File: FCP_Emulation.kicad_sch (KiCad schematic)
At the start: 92 parts, among them J1 Conn_01x10_Female, J2 Conn_01x10_Female, J3 Conn_01x10_Female, J4 Conn_01x02_Female, J5 Conn_01x02_Female, U2 LM2902

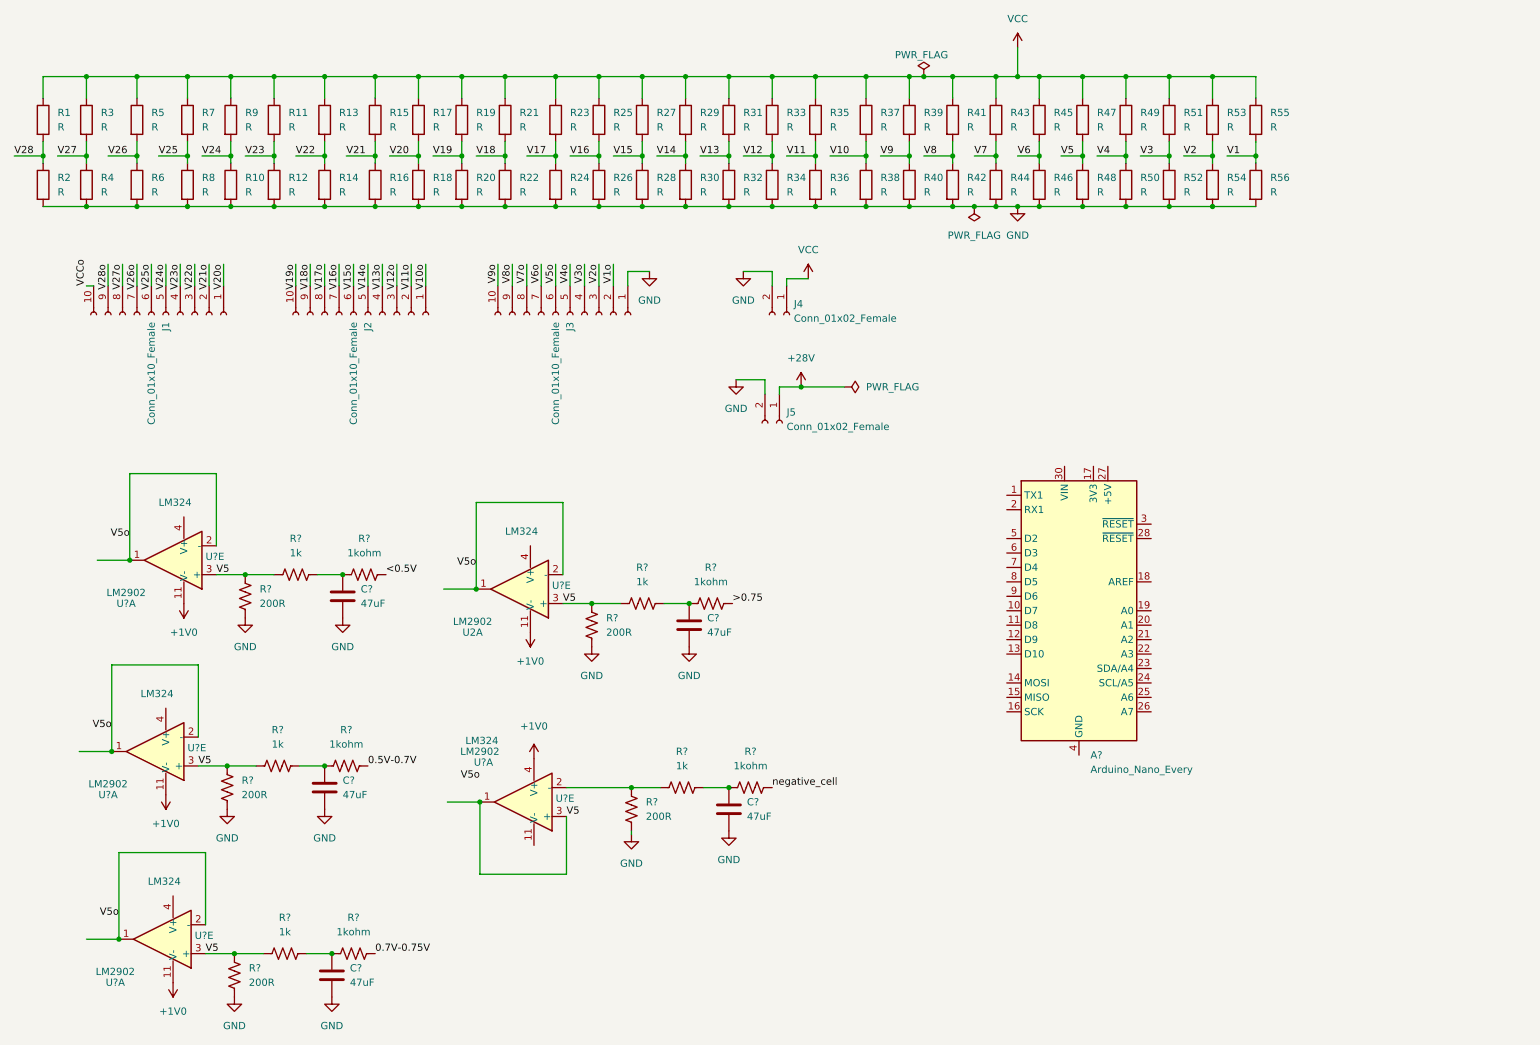
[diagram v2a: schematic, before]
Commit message: changed op amp circuit values based on breadboarding and simualtion
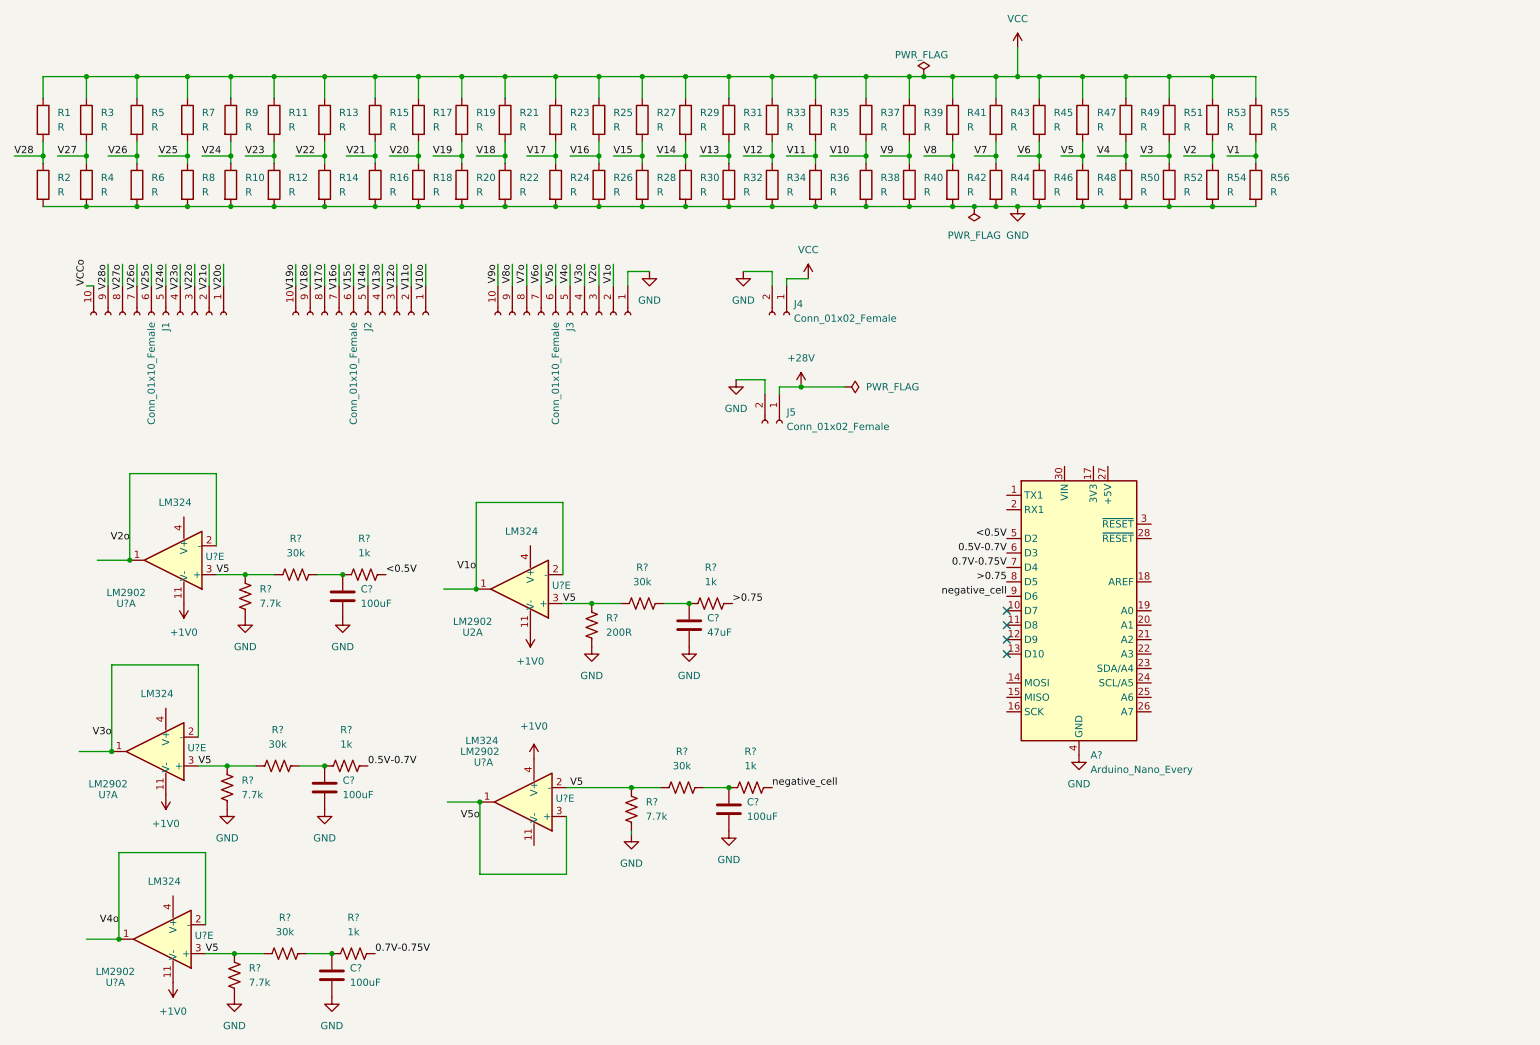
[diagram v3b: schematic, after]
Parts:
- C? (x4): value 47uF -> 100uF
- R? (x5): value 1kohm -> 1k
- R? (x4): value 200R -> 7.7k
- R? (x5): value 1k -> 30k
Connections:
- net 0.5V-0.7V: now also A?.6 (D3)
- net 0.7V-0.75V: now also A?.7 (D4)
- net <0.5V: now also A?.5 (D2)
- net >0.75: now also A?.8 (D5)
- net GND: now also A?.29 (GND), A?.4 (GND)
- net V1o: now also U2.1, U2.2 (-)
- net V2o: now also U?.1, U?.2 (-)
- net V3o: now also U?.1, U?.2 (-)
- net V4o: now also U?.1, U?.2 (-)
- net V5: now also R?.1, R?.1, U?.2 (-); no longer U?.1, U?.3 (+)
- net V5o: now also U?.1, U?.3 (+); no longer U2.1, U2.2 (-), U?.1, U?.1, U?.1, U?.2 (-), U?.2 (-), U?.2 (-)
- net negative_cell: now also A?.9 (D6)
- no-connect marks 0 -> 4

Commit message: added negative case schematic
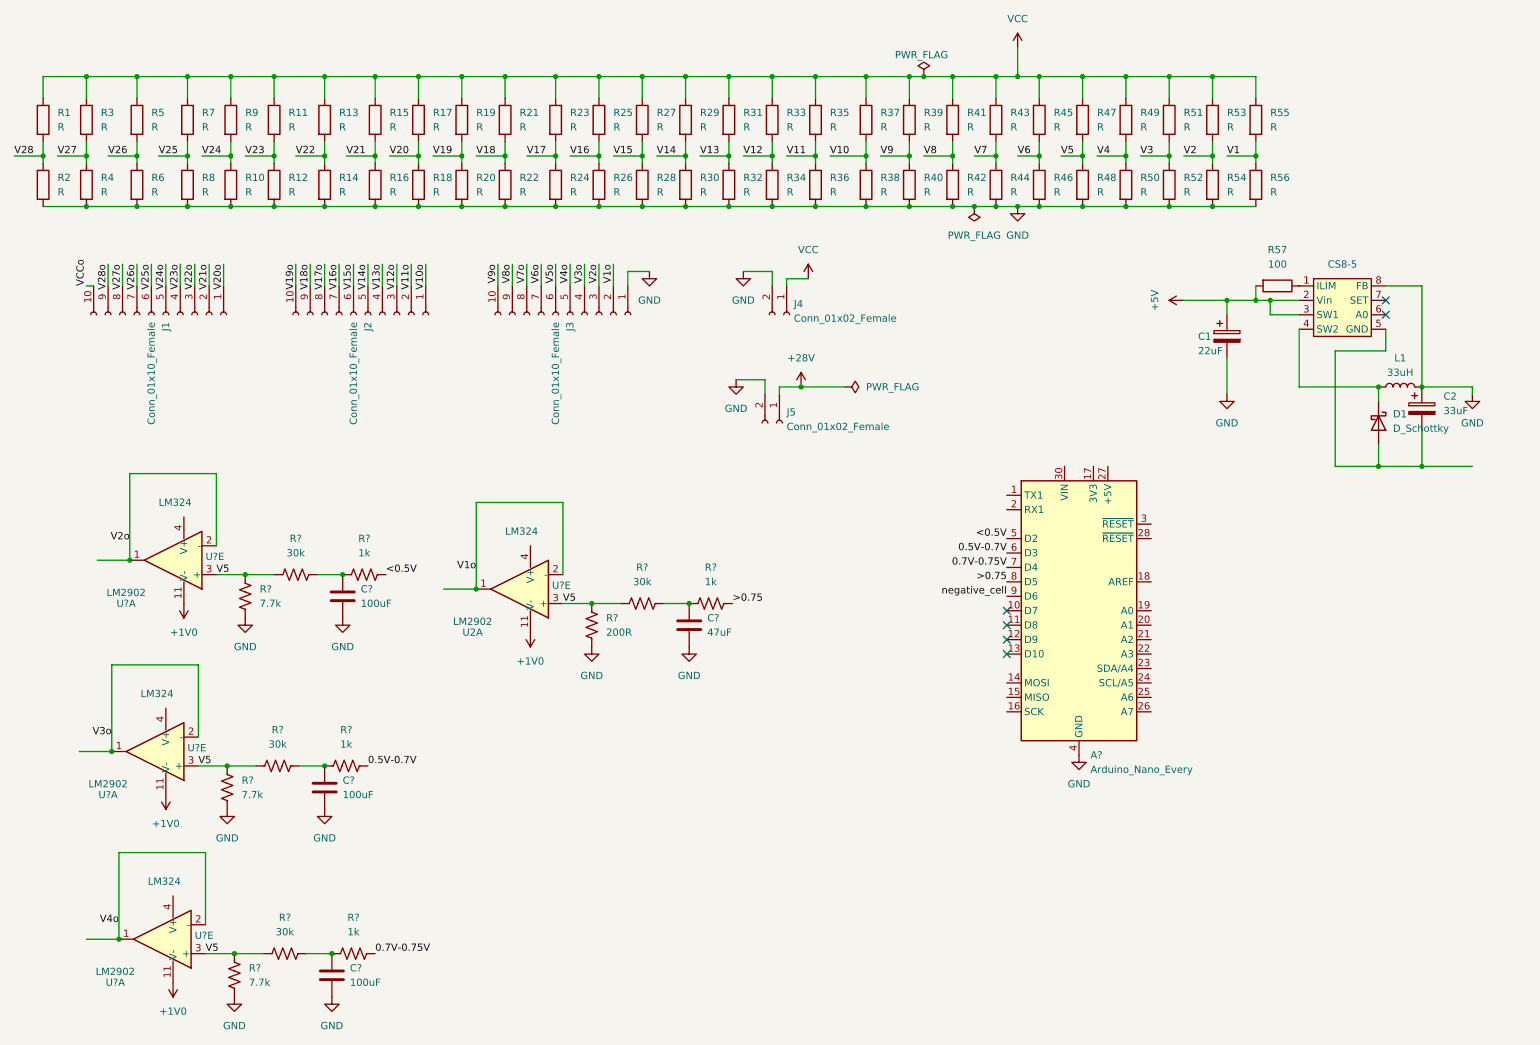
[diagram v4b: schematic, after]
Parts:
- removed C?: 100uF, symbol Device:C
- removed R?: 1k, symbol Device:R_US
- removed R?: 7.7k, symbol Device:R_US
- removed R?: 30k, symbol Device:R_US
- removed U?: LM2902, Package_SO:SO-14_3.9x8.65mm_P1.27mm, symbol Amplifier_Operational:LM2902
- removed U?: LM324, symbol Amplifier_Operational:LM324
- added C1: 22uF, symbol Device:C_Polarized
- added C2: 33uF, symbol Device:C_Polarized
- added CS8-5: ~, symbol lt1111:LT1111CN8-5
- added D1: D_Schottky, symbol Device:D_Schottky
- added L1: 33uH, symbol Device:L
- added R57: 100, symbol Device:R
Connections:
- net GND: now also C1.2, C2.1, CS8-5.8 (FB), L1.2
- new net: CS8-5.1 (ILIM), R57.1
- new net: CS8-5.4 (SW2), D1.1 (K), L1.1
- new net: C2.2, CS8-5.5 (GND), D1.2 (A)
- new net +5V: C1.1, CS8-5.2 (Vin), CS8-5.3 (SW1), R57.2
- no-connect marks 4 -> 6

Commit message: added voltage divider on negative case
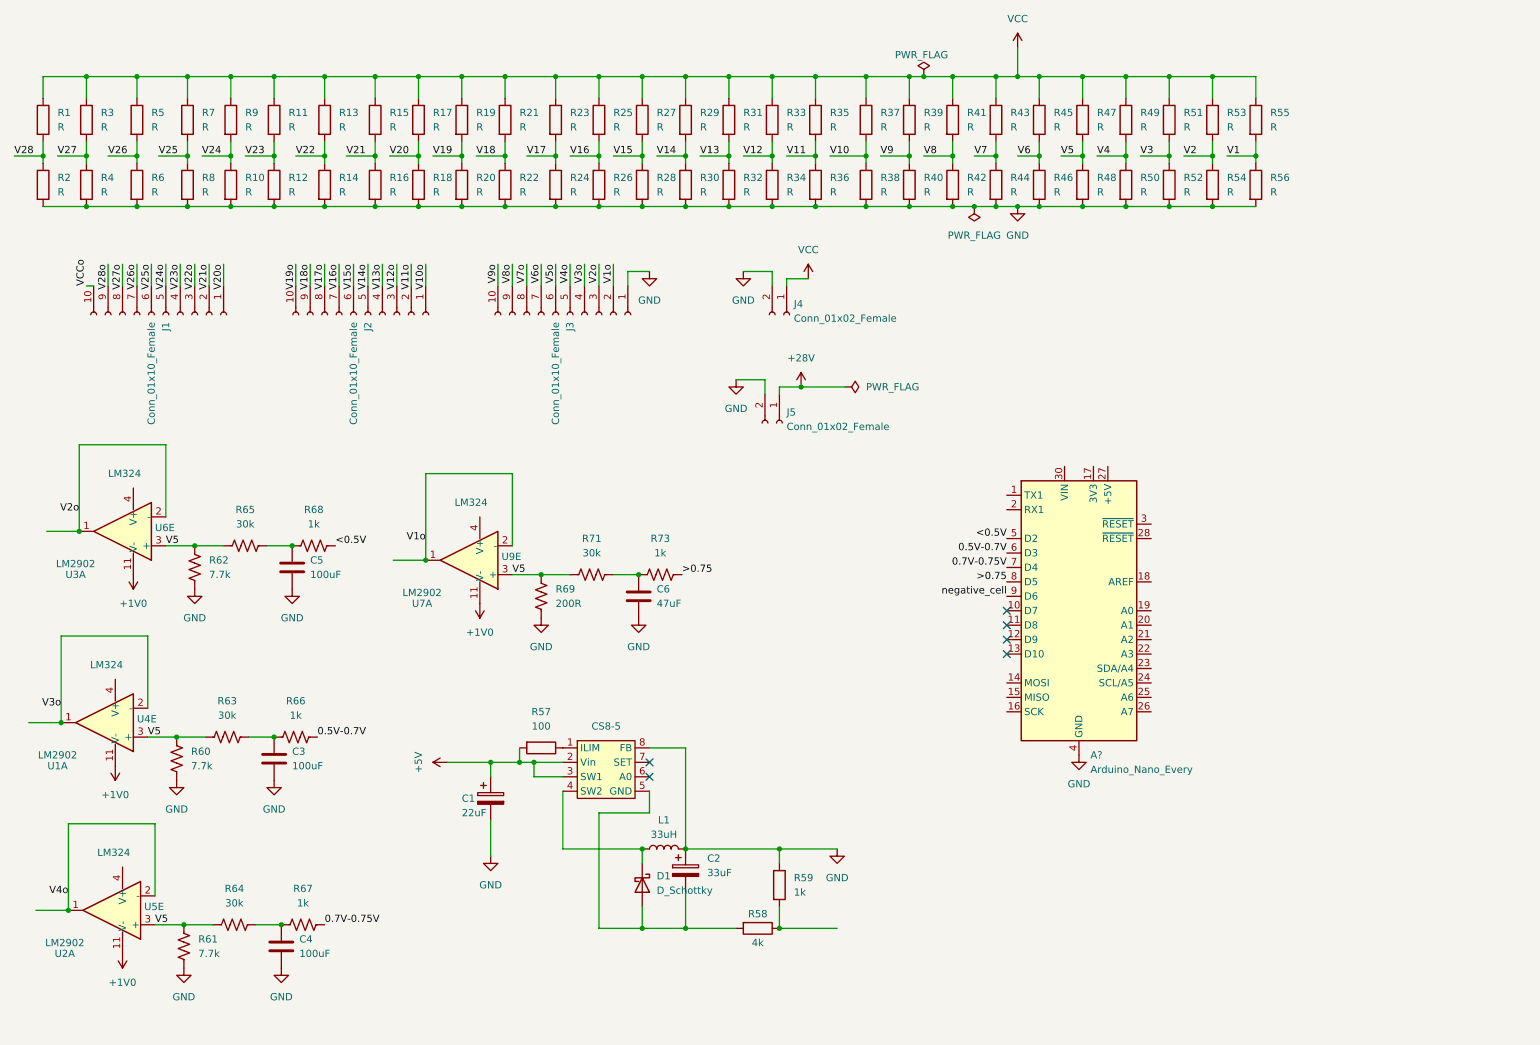
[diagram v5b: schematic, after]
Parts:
- removed C?: 47uF, symbol Device:C
- removed C? (x3): 100uF, symbol Device:C
- removed R? (x4): 1k, symbol Device:R_US
- removed R? (x3): 7.7k, symbol Device:R_US
- removed R? (x4): 30k, symbol Device:R_US
- removed R?: 200R, symbol Device:R_US
- removed U? (x4): LM324, symbol Amplifier_Operational:LM324
- removed U? (x3): LM2902, Package_SO:SO-14_3.9x8.65mm_P1.27mm, symbol Amplifier_Operational:LM2902
- added C3, C4, C5: 100uF, symbol Device:C
- added C6: 47uF, symbol Device:C
- added R58: 4k, symbol Device:R
- added R59: 1k, symbol Device:R
- added R60, R61, R62: 7.7k, symbol Device:R_US
- added R63, R64, R65, R71: 30k, symbol Device:R_US
- added R66, R67, R68, R73: 1k, symbol Device:R_US
- added R69: 200R, symbol Device:R_US
- added U1, U3, U7: LM2902, Package_SO:SO-14_3.9x8.65mm_P1.27mm, symbol Amplifier_Operational:LM2902
- added U4, U5, U6, U9: LM324, symbol Amplifier_Operational:LM324
- CS8-5: footprint (none) -> Package_SO:SOIC-8_3.9x4.9mm_P1.27mm
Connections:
- net +1V0: now also U4.11 (V-), U5.11 (V-), U6.11 (V-), U9.11 (V-)
- net 0.5V-0.7V: now also R66.2
- net 0.7V-0.75V: now also R67.2
- net <0.5V: now also R68.2
- net >0.75: now also R73.2
- net GND: now also C3.2, C4.2, C5.2, C6.2, R59.1, R60.2, R61.2, R62.2, R69.2
- net V1o: now also U7.1, U7.2 (-); no longer U2.1, U2.2 (-)
- net V2o: now also U3.1, U3.2 (-)
- net V3o: now also U1.1, U1.2 (-)
- net V4o: now also U2.1, U2.2 (-)
- net V5: now also R60.1, R61.1, R62.1, R63.1, R64.1, R65.1, R69.1, R71.1, U1.3 (+), U3.3 (+), U7.3 (+)
- net at C2.2, CS8-5.5 (GND), D1.2 (A): now also R58.2
- new net: C6.1, R71.2, R73.1
- new net: R58.1, R59.2
- new net: C3.1, R63.2, R66.1
- new net: C5.1, R65.2, R68.1
- new net: C4.1, R64.2, R67.1
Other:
- moved on the sheet: C1, C2, CS8-5, D1, L1, R57

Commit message: Specced out negative case circuit
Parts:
- C1: footprint (none) -> Capacitor_Tantalum_SMD:CP_EIA-7343-40_Kemet-Y
- C2: footprint (none) -> Capacitor_Tantalum_SMD:CP_EIA-3528-21_Kemet-B
- D1: footprint (none) -> Diode_SMD:D_SMB
- R57, R58, R59: footprint (none) -> Resistor_SMD:R_01005_0402Metric
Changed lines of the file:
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@@
       (effects (font (size 1.27 1.27)))
     )
-    (property "Footprint" "" (at 106.68 144.272 90)
-      (effects (font (size 1.27 1.27)) hide)
-    )
-    (property "Datasheet" "~" (at 106.68 146.05 0)
+    (property "Footprint" "Resistor_SMD:R_01005_0402Metric" (at 106.68 144.272 90)
+      (effects (font (size 1.27 1.27)) hide)
+    )
+    (property "Datasheet" "https://www.seielect.com/catalog/sei-rmcf_rmcp.pdf" (at 106.68 146.05 0)
       (effects (font (size 1.27 1.27)) hide)
     )
@@
       (effects (font (size 1.27 1.27)))
     )
-    (property "Footprint" "" (at 144.78 176.022 90)
-      (effects (font (size 1.27 1.27)) hide)
-    )
-    (property "Datasheet" "~" (at 144.78 177.8 0)
+    (property "Footprint" "Resistor_SMD:R_01005_0402Metric" (at 144.78 176.022 90)
+      (effects (font (size 1.27 1.27)) hide)
+    )
+    (property "Datasheet" "https://www.seielect.com/catalog/sei-rmcf_rmcp.pdf" (at 144.78 177.8 0)
       (effects (font (size 1.27 1.27)) hide)
     )
@@
       (effects (font (size 1.27 1.27)) (justify left))
     )
-    (property "Footprint" "" (at 124.46 170.18 0)
-      (effects (font (size 1.27 1.27)) hide)
-    )
-    (property "Datasheet" "~" (at 124.46 170.18 0)
+    (property "Footprint" "Diode_SMD:D_SMB" (at 124.46 170.18 0)
+      (effects (font (size 1.27 1.27)) hide)
+    )
+    (property "Datasheet" "~https://www.vishay.com/docs/95746/vs-mbrs130-m3.pdf" (at 124.46 170.18 0)
       (effects (font (size 1.27 1.27)) hide)
     )
@@
       (effects (font (size 1.27 1.27)) (justify left))
     )
-    (property "Footprint" "" (at 146.812 170.18 90)
-      (effects (font (size 1.27 1.27)) hide)
-    )
-    (property "Datasheet" "~" (at 148.59 170.18 0)
+    (property "Footprint" "Resistor_SMD:R_01005_0402Metric" (at 146.812 170.18 90)
+      (effects (font (size 1.27 1.27)) hide)
+    )
+    (property "Datasheet" "https://www.seielect.com/catalog/sei-rmcf_rmcp.pdf" (at 148.59 170.18 0)
       (effects (font (size 1.27 1.27)) hide)
     )
@@
       (effects (font (size 1.27 1.27)) (justify left))
     )
-    (property "Footprint" "" (at 98.7552 158.75 0)
-      (effects (font (size 1.27 1.27)) hide)
-    )
-    (property "Datasheet" "~" (at 97.79 154.94 0)
+    (property "Footprint" "Capacitor_Tantalum_SMD:CP_EIA-7343-40_Kemet-Y" (at 98.7552 158.75 0)
+      (effects (font (size 1.27 1.27)) hide)
+    )
+    (property "Datasheet" "~https://connect.kemet.com:7667/gateway/IntelliData-ComponentDocumentation/1.0/download/specsheet/T521D226M035ATE060" (at 97.79 154.94 0)
       (effects (font (size 1.27 1.27)) hide)
     )
@@
       (effects (font (size 1.27 1.27)) hide)
     )
-    (property "Datasheet" "~" (at 128.27 163.83 0)
+    (property "Datasheet" "~https://products.sumida.com/products/pdf/CDPH4D19F.pdf" (at 128.27 163.83 0)
       (effects (font (size 1.27 1.27)) hide)
     )
@@
       (effects (font (size 1.27 1.27)) (justify left))
     )
-    (property "Footprint" "" (at 133.0452 171.45 0)
-      (effects (font (size 1.27 1.27)) hide)
-    )
-    (property "Datasheet" "~" (at 132.08 167.64 0)
-      (effects (font (size 1.27 1.27)) hide)
-    )
+    (property "Footprint" "Capacitor_Tantalum_SMD:CP_EIA-3528-21_Kemet-B" (at 133.0452 171.45 0)
+      (effects (font (size 1.27 1.27)) hide)
+    )
+    (property "Datasheet" "~https://connect.kemet.com:7667/gateway/IntelliData-ComponentDocumentation/1.0/download/specsheet/T520B336M010ATE040" (at 132.08 167.64 0)
+      (effects (font (size 1.27 1.27)) hide)
+    )
